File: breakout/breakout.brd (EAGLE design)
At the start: 30 x 30.2 mm, 34 parts, among them X1 PCIE-MINI-CONN

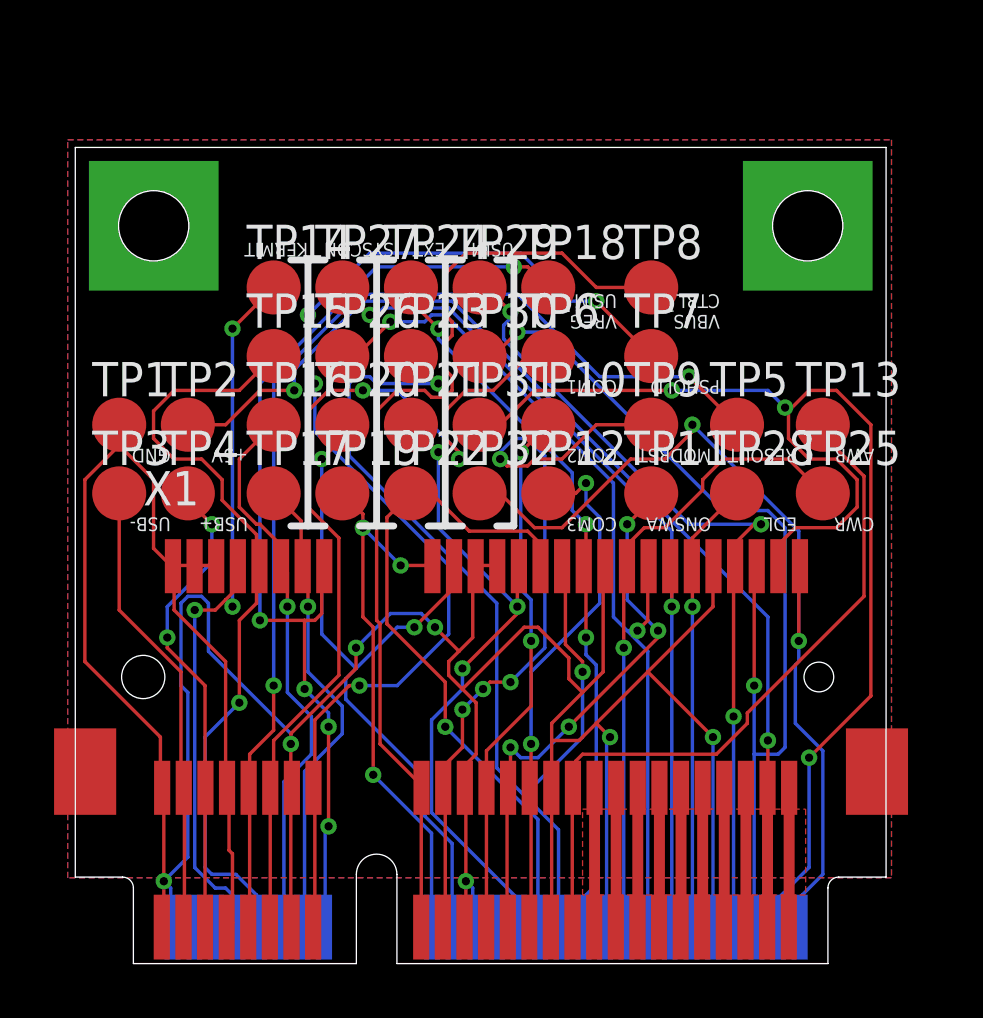
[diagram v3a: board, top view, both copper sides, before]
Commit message: Resize both boards
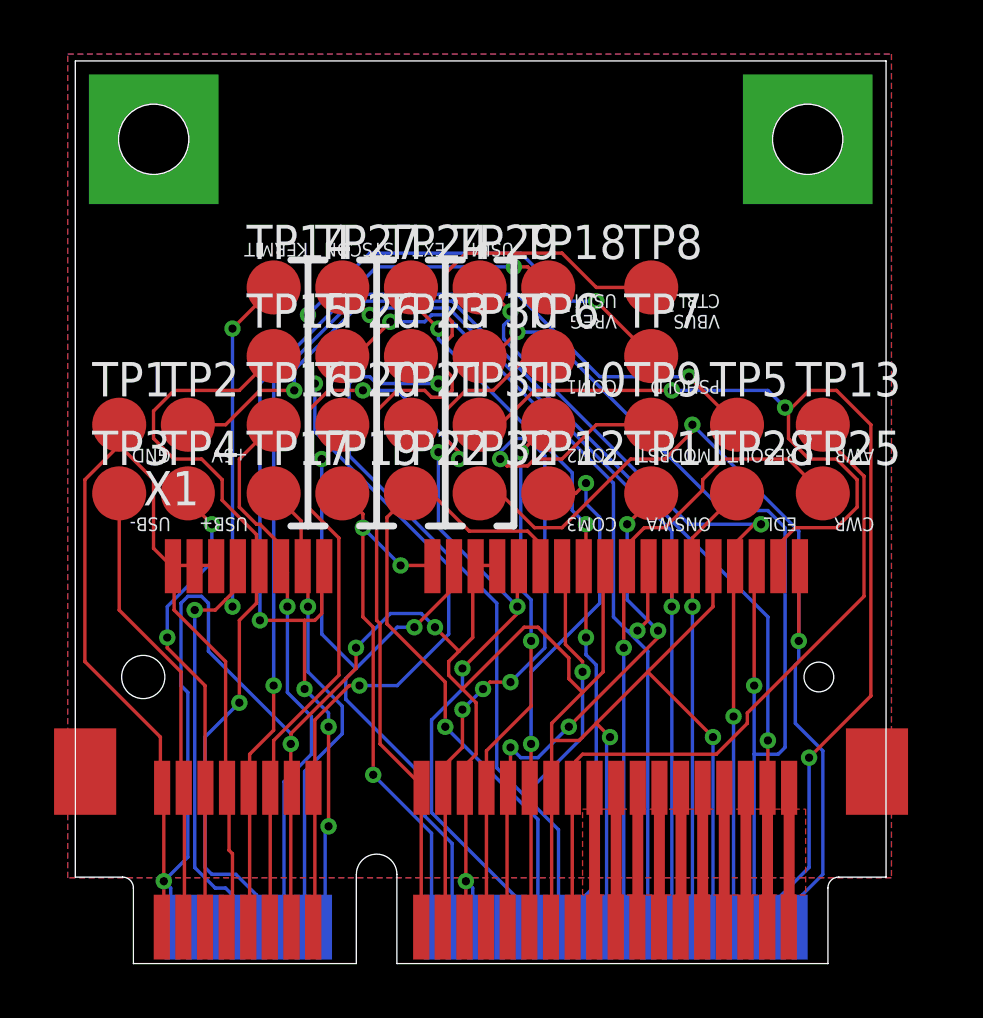
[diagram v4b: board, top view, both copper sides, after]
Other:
- board size 30 x 30.2 mm -> 30 x 33.4 mm
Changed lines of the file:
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@@
 <wire x1="30.226" y1="6.477" x2="30.23" y2="6.43" width="0.127" layer="16"/>
 <polygon width="0.4064" layer="1" rank="2">
-<vertex x="6.35" y="35.56"/>
-<vertex x="36.83" y="35.56"/>
+<vertex x="6.35" y="38.735"/>
+<vertex x="36.83" y="38.735"/>
 <vertex x="36.83" y="8.255"/>
 <vertex x="6.35" y="8.255"/>
 </polygon>
 <polygon width="0.4064" layer="16">
-<vertex x="6.35" y="35.56"/>
-<vertex x="36.83" y="35.56"/>
+<vertex x="6.35" y="38.735"/>
+<vertex x="36.83" y="38.735"/>
 <vertex x="36.83" y="8.255"/>
 <vertex x="6.35" y="8.255"/>
@@
 <contactref element="U$1" pad="GND@1"/>
 <contactref element="U$1" pad="GND@2"/>
+<wire x1="30.244" y1="19.7845" x2="33.73" y2="35.58" width="0" layer="19" extent="1-1"/>
+<wire x1="9.53" y1="35.58" x2="8.255" y2="25.019" width="0" layer="19" extent="1-1"/>
 </signal>
 <signal name="USB_N">
